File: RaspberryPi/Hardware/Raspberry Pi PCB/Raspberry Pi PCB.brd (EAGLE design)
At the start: 45 x 60 mm, 32 parts, among them Q11 BSS138, Q12 BSS138, Q2 BSS138

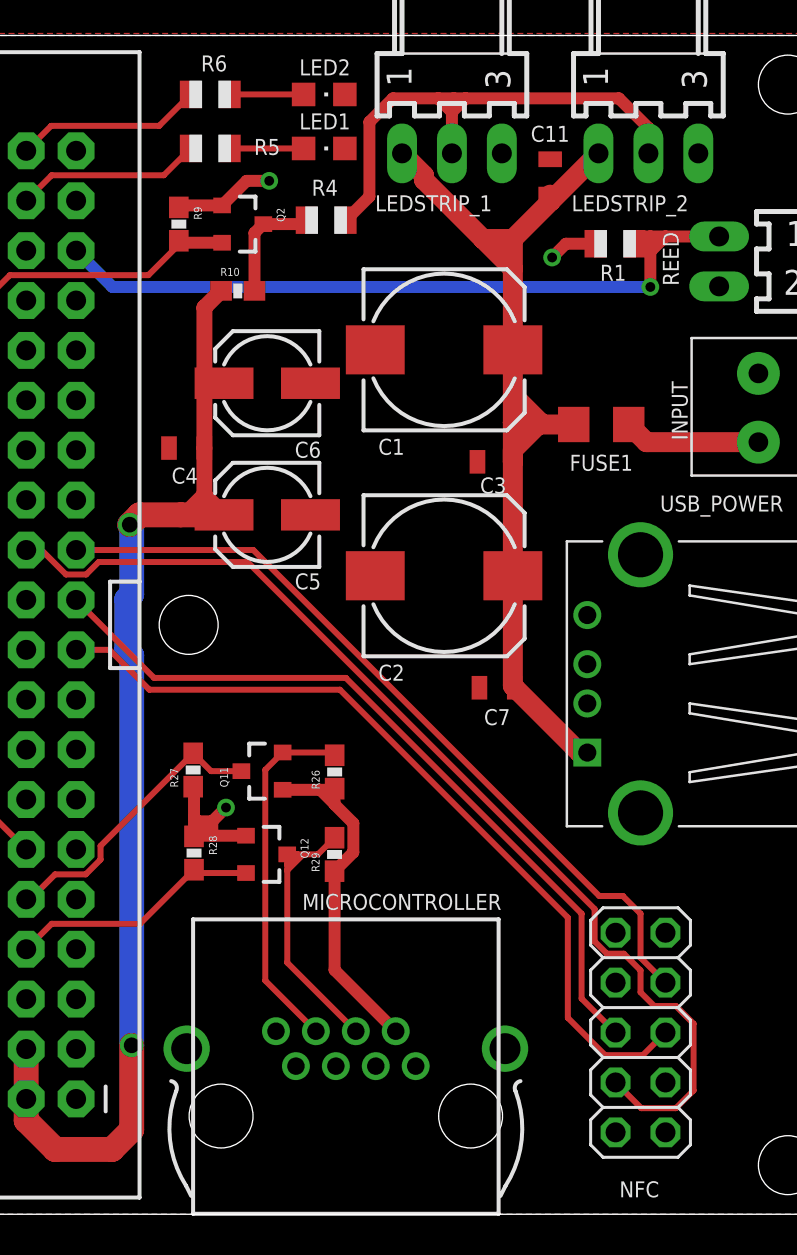
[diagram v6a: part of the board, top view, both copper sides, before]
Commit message: Finished the first version of the Raspberry PCB.
Design rule check worked out fine. The PCB should now be ready for ordering.
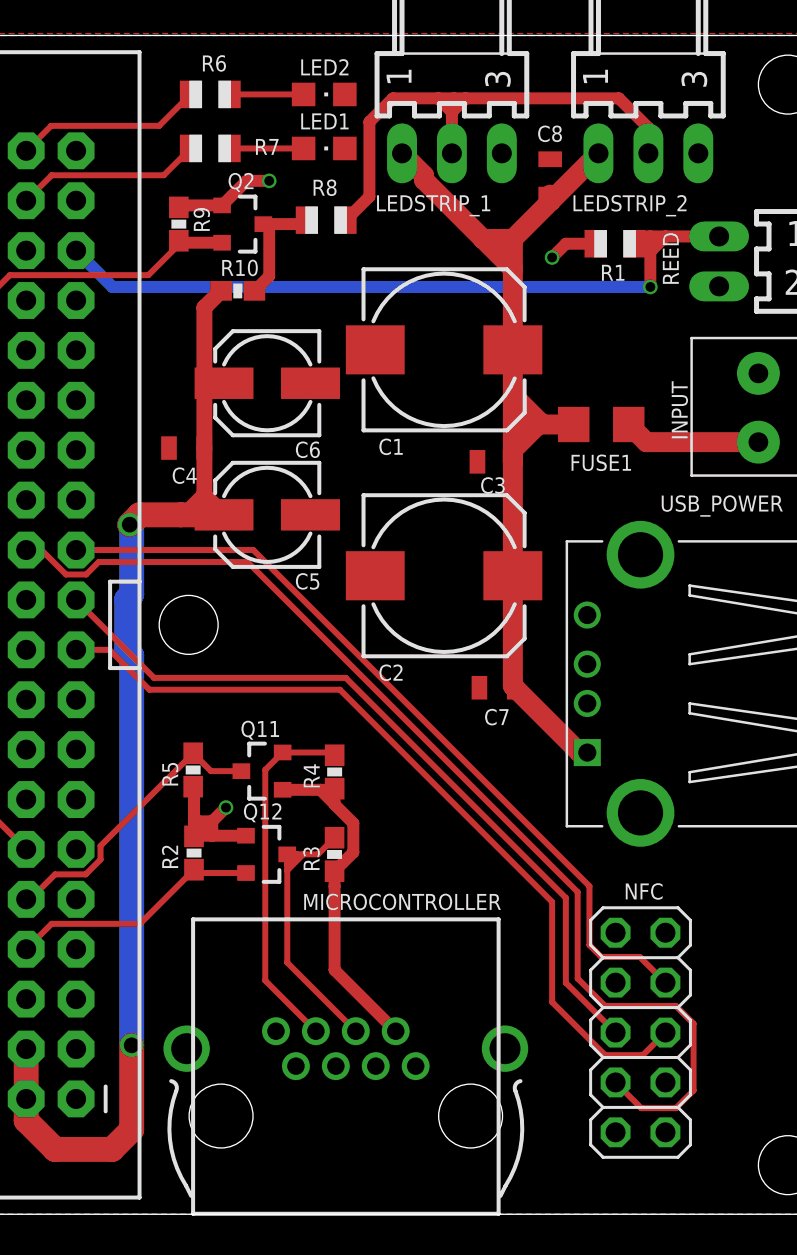
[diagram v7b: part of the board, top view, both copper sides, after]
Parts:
- removed R26, R27: 10K, SparkFun:0603-RES
- added R7, R8: (no value), adafruit:R0805
- R4, R5: value (none) -> 10K; device adafruit:R0805 -> SparkFun:0603-RES
- moved R5 31.6 mm to (12.2, 22.6), turned to 90 degrees
- moved R4 28.1 mm to (19.4, 22.5), turned to 90 degrees
- renumbered C11 to C8, R28 to R2, R29 to R3
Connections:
- net +12V: now also R4.1; no longer R26.1
- net 3.3V: now also R5.1; no longer R27.1
- net LED_1: now also R7.1; no longer R5.1
- net N$3: now also R8.1; no longer R4.1
- net N$5: now also R7.2; no longer R5.2
- net RX_RASPI: now also R5.2; no longer R27.2
- net TX_ATXMEGA: now also R4.2; no longer R26.2
- net WS2811_DATA_5V: now also R8.2; no longer R4.2
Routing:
- net SPI_CS: track 54.4 -> 55.3 mm
- net +12V: track 18.1 -> 18.9 mm

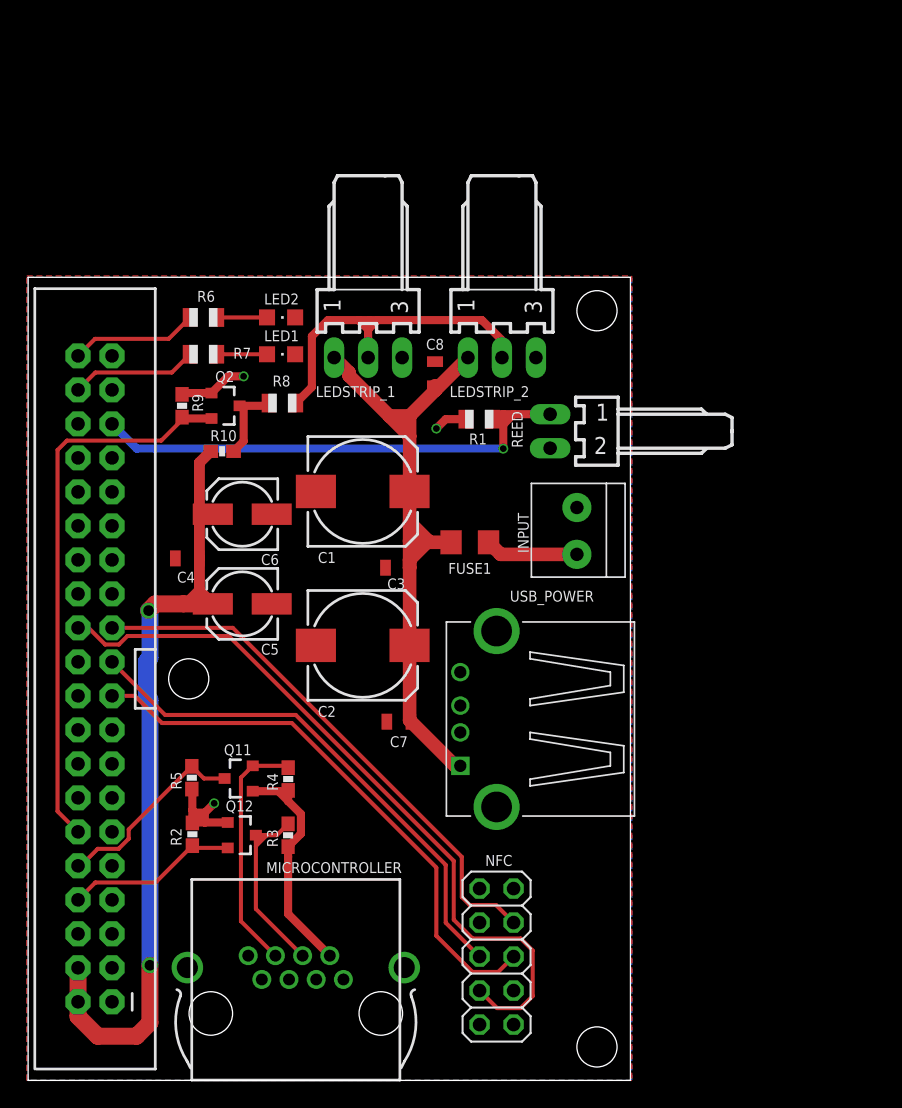
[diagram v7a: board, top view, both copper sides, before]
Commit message: The Raspberry PCB is almost finished now.
The buttons and the jumper has been included. The size has been increased. All the primary functionality has been finished now.
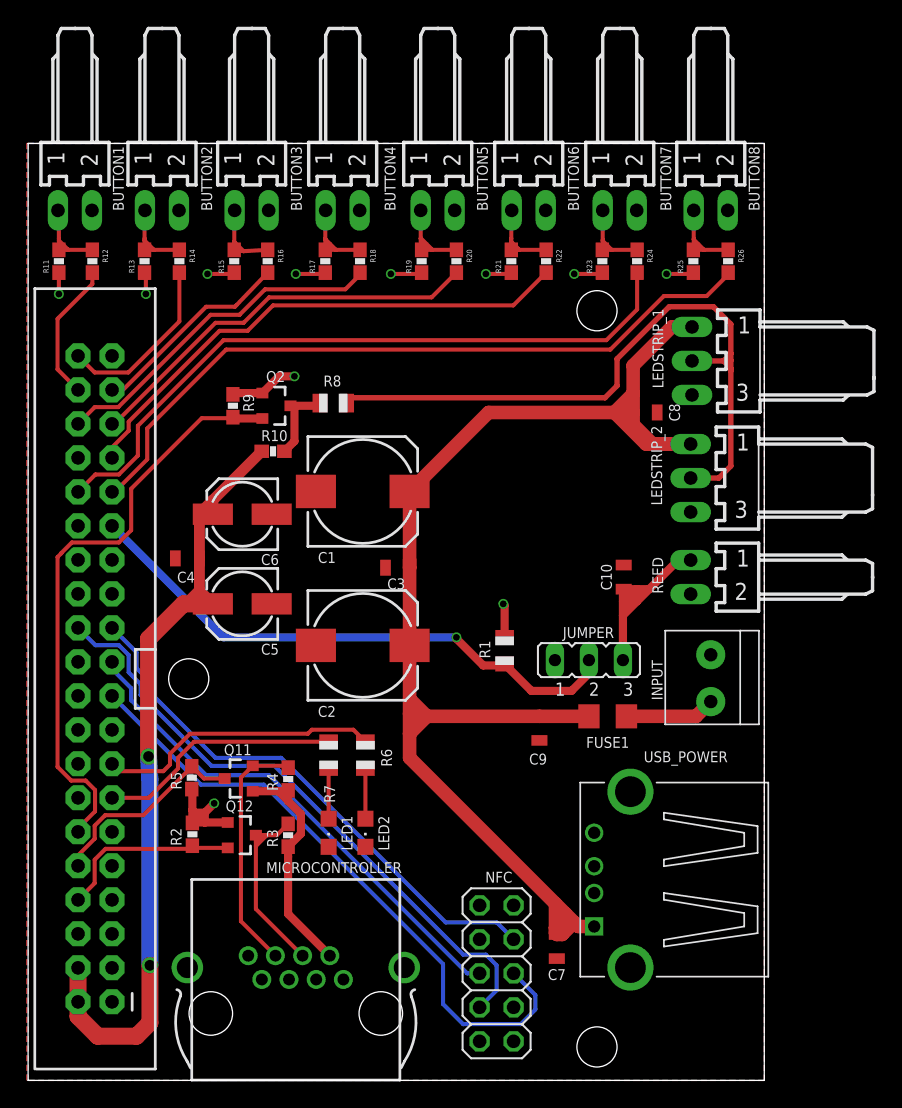
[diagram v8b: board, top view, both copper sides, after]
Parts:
- added BUTTON1, BUTTON2, BUTTON3, BUTTON4, BUTTON5, BUTTON6, BUTTON7, BUTTON8: 22-05-7028-02, con-molex:7395-02
- added C10, C9: 100nF, SparkFun-Capacitors:0805
- added JUMPER: (no value), jumper:JP2
- added R11, R12, R13, R14, R15, R16, R17, R18, R19, R20, R21, R22, R23, R24, R25, R26: 10K, SparkFun:0603-RES
- moved LED2 39.0 mm to (25.2, 18.5), turned to 180 degrees
- moved LED1 35.9 mm to (22.4, 18.5), turned to 180 degrees
- moved R6 34.9 mm to (25.2, 24.3), turned to 270 degrees
- moved R7 31.4 mm to (22.4, 24.3), turned to 270 degrees
- moved LEDSTRIP_1 24.2 mm to (49.6, 53.8), turned to 90 degrees
- moved C7 20.5 mm to (39.5, 10.0), turned to 270 degrees
- moved R1 17.4 mm to (35.6, 32.1), turned to 90 degrees
- moved LEDSTRIP_2 16.7 mm to (49.5, 45.0), turned to 90 degrees
- moved FUSE1 16.6 mm to (43.3, 27.2)
- moved C8 16.0 mm to (46.1, 49.9), turned to 0 degrees
- moved USB_POWER 15.6 mm to (45.0, 15.0)
- moved REED 15.1 mm to (49.5, 37.6)
- moved INPUT 14.9 mm to (51.0, 30.0)
- moved Q2 3.80 mm to (18.5, 50.4)
- moved R10 3.80 mm to (18.3, 47.0)
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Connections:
- removed net GP12: JP2.32
- removed net GP13: JP2.33
- removed net GP16: JP2.36
- removed net GP22: JP2.15
- removed net GP26: JP2.37
- removed net GP27: JP2.13
- removed net GP5: JP2.29
- removed net GP6: JP2.31
- new net BUTTON1: JP2.38, R12.2
- new net BUTTON2: JP2.40, R14.2
- new net BUTTON3: JP2.37, R16.2
- new net BUTTON4: JP2.36, R18.2
- new net BUTTON5: JP2.35, R20.2
- new net BUTTON6: JP2.33, R22.2
- new net BUTTON7: JP2.32, R24.2
- new net BUTTON8: JP2.31, R26.2
- new net N$1: C10.1, JUMPER.3, REED.1
- new net N$10: BUTTON6.1, R21.2, R22.1
- new net N$11: BUTTON7.1, R23.2, R24.1
- new net N$12: BUTTON8.1, R25.2, R26.1
- new net N$2: BUTTON2.1, R13.2, R14.1
- new net N$6: BUTTON1.1, R11.2, R12.1
- new net N$7: BUTTON3.1, R15.2, R16.1
- new net N$8: BUTTON4.1, R17.2, R18.1
- new net N$9: BUTTON5.1, R19.2, R20.1
- net 3.3V: now also R11.1, R13.1, R15.1, R17.1, R19.1, R21.1, R23.1, R25.1
- net 5V_USB: now also C9.1
- net GND: now also BUTTON1.2, BUTTON2.2, BUTTON3.2, BUTTON4.2, BUTTON5.2, BUTTON6.2, BUTTON7.2, BUTTON8.2, C10.2, C9.2, JUMPER.1
- net LED_1: now also JP2.13; no longer JP2.38
- net LED_2: now also JP2.15; no longer JP2.40
- net REED_SWITCH: now also JP2.29, JUMPER.2; no longer JP2.35, REED.1
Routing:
- net BUTTON8: track 0.00 -> 54.2 mm
- net 5V_USB: track 52.5 -> 106.2 mm
- net BUTTON7: track 0.00 -> 51.5 mm
- net BUTTON6: track 0.00 -> 39.0 mm
- net BUTTON5: track 0.00 -> 30.4 mm
- net BUTTON4: track 0.00 -> 25.8 mm
- net WS2811_DATA_5V: track 26.9 -> 51.8 mm
- net N$1: track 0.00 -> 17.2 mm
- net 3.3V: track 17.9 -> 33.9 mm, vias 3 -> 11
- net BUTTON3: track 0.00 -> 15.3 mm
- net BUTTON2: track 0.00 -> 13.3 mm
- net LED_2: track 9.56 -> 21.3 mm
- net BUTTON1: track 0.00 -> 10.5 mm
- net LED_1: track 9.47 -> 18.4 mm
- net SPI_CS: track 55.3 -> 46.6 mm
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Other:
- board size 45 x 60 mm -> 55 x 70 mm
- board text added: "Bidondispenser 4.0"
- board text added: "Glen te Hofsté"
- board text added: "Raspberry Pi PCB version 1.0"
